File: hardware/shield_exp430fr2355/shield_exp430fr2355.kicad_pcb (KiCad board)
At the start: 2 copper layers, 34.3 x 50.8 mm, 51 parts, among them J1 TI_BOOSTER_40_J1, J10 Conn_01x02_Male, J11 Conn_01x04_Male, J12 Conn_01x02_Male, J13 Conn_01x02_Male, J14 Conn_01x02_Male, J15 Conn_01x02_Male, J16 Conn_01x02_Male, J17 Conn_01x02_Male, J18 Conn_01x02_Male, J19 Conn_01x02_Male, J2 TI_BOOSTER_40_J2, J20 Conn_01x02_Male, J21 Conn_01x02_Male, J22 Conn_01x02_Male, J23 Conn_01x02_Male, J24 Conn_01x02_Male, J25 Conn_01x02_Male, J27 Conn_01x02_Male, J28 Conn_01x02_Male, J3 TI_BOOSTER_40_J3, J4 TI_BOOSTER_40_J4, J6 Conn_02x13_Odd_Even, J7 Conn_01x02_Male, J8 Conn_01x02_Male, J9 Conn_01x02_Male, Q1 2N7002, Q2 2N7002, U1 NCP1117-3.3_SOT223

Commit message: Finished schematic
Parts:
- removed J11: Conn_01x04_Male, Connector_PinHeader_2.54mm:PinHeader_1x04_P2.54mm_Vertical
- D3, D4, U1: moved to B.Cu
- moved J12 157.1 mm to (309.6, 150.1)
- moved J21 145.8 mm to (308.9, 131.8)
- moved R14 144.5 mm to (267.8, 175.0)
- moved D1 143.6 mm to (314.6, 152.0)
- moved R15 143.3 mm to (267.7, 171.2)
- moved D2 139.2 mm to (314.5, 134.5)
- moved J28 128.1 mm to (256.0, 172.7)
- moved Q2 122.7 mm to (262.9, 174.1)
- moved J23 110.5 mm to (278.9, 128.7)
- moved J22 110.2 mm to (278.9, 120.0)
- moved R11 107.5 mm to (283.3, 127.9), turned to 180 degrees
- moved R7 105.4 mm to (283.3, 131.2)
- moved R10 100.3 mm to (282.4, 122.4), turned to 180 degrees
- moved R6 97.3 mm to (282.6, 119.8)
- moved R12 92.5 mm to (214.5, 160.3)
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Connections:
- net Net-(J1-Pad5) renamed P3.6
- net Net-(J1-Pad6) renamed P5.2
- net Net-(J1-Pad7) renamed P4.5
- net Net-(J1-Pad8) renamed P3.4
- net Net-(J2-Pad10) renamed P3.0
- net Net-(J2-Pad4) renamed P4.0
- net Net-(J2-Pad5) renamed RST
- net Net-(J2-Pad6) renamed P4.6
- net Net-(J2-Pad7) renamed P4.7
- net Net-(J2-Pad8) renamed P4.4
- net Net-(J3-Pad10) renamed P3.1
- net Net-(J3-Pad4) renamed P5.3
- net Net-(J3-Pad9) renamed P3.5
- net Net-(J4-Pad10) renamed P3.2
- net Net-(J4-Pad6) renamed P6.4
- net Net-(J4-Pad7) renamed P3.7
- net Net-(J4-Pad9) renamed P3.3
- D1 pad 3: P1.0 -> P1.1
- D2 pad 3: P1.3 -> P1.2
- J1 pad 1: VCC -> +3V3
- J1 pad 10: Net-(J1-Pad10) -> P1.2
- J1 pad 2: Net-(J1-Pad2) -> P1.5
- J1 pad 3: Net-(J1-Pad3) -> P1.6
- J1 pad 4: Net-(J1-Pad4) -> P1.7
- J1 pad 9: Net-(J1-Pad9) -> P1.3
- J12 pad 2: P1.0 -> P1.1
- J14 pad 2: P1.4 -> P2.2
- J15 pad 2: P2.1 -> P6.0
- J16 pad 2: P2.2 -> P6.1
- J17 pad 2: P2.4 -> P6.2
- J18 pad 2: P2.5 -> P6.3
- J2 pad 2: Net-(J2-Pad2) -> P2.0
- J2 pad 3: Net-(J2-Pad3) -> P2.2
- J2 pad 9: Net-(J2-Pad9) -> P2.5
- J20 pad 2: P1.7 -> P2.3
- J21 pad 2: P1.3 -> P1.2
- J24 pad 2: P2.0 -> P5.4
- J25 pad 2: P2.3 -> P2.4
- J3 pad 3: Net-(J3-Pad3) -> P1.4
- J3 pad 5: Net-(J3-Pad5) -> P5.1
- J3 pad 6: Net-(J3-Pad6) -> P5.0
- J3 pad 7: Net-(J3-Pad7) -> P5.4
- J3 pad 8: Net-(J3-Pad8) -> P1.1
- J4 pad 1: Net-(J4-Pad1) -> P2.1
- J4 pad 2: Net-(J4-Pad2) -> P6.0
- J4 pad 3: Net-(J4-Pad3) -> P6.1
- J4 pad 4: Net-(J4-Pad4) -> P6.2
- J4 pad 5: Net-(J4-Pad5) -> P6.3
- J4 pad 8: Net-(J4-Pad8) -> P2.4
- Q1 pad 2: P1.2 -> P1.7
- Q2 pad 2: P1.1 -> P1.6
- R1 pad 2: P1.5 -> P2.0
- R10 pad 1: P2.6 -> P5.0
- R11 pad 1: P2.7 -> P5.1
- R12 pad 2: P1.2 -> P1.7
- R14 pad 2: P1.1 -> P1.6
- R3 pad 1: P1.5 -> P2.0
- R4 pad 2: P1.6 -> P2.1
- R5 pad 1: P1.6 -> P2.1
- R6 pad 2: P2.6 -> P5.0
- R7 pad 2: P2.7 -> P5.1
- R8 pad 1: P2.0 -> P5.4
- R9 pad 1: P2.3 -> P2.4
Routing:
- net PWM1: track 0.00 -> 83.4 mm
- net PWM1N: track 0.00 -> 81.0 mm
- net PWM2: track 0.00 -> 76.4 mm
- net PWM2N: track 0.00 -> 75.6 mm
- net +5V: track 0.00 -> 47.9 mm
- net Net-(C1-Pad1): track 0.00 -> 24.2 mm
- net +3V3: track 0.00 -> 13.2 mm, vias 0 -> 2
- net P6.3: track 0.00 -> 5.35 mm
- net P6.2: track 0.00 -> 5.14 mm
- net P6.1: track 0.00 -> 4.92 mm
- net P6.0: track 0.00 -> 4.73 mm
- net GND: track 0.00 -> 3.59 mm
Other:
- board size 34.3 x 50.8 mm -> 74.6 x 50 mm
- net class Default: clearance 0.254 -> 0.3048; trace_width 0.254 -> 0.508; via_dia 0.889 -> 1.5; via_drill 0.635 -> 0.6
- rule trace_clearance: 0.254 -> 0.3048

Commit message: Routing tracks
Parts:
- C1, C2, D1, D2, Q1, Q2, R1, R10, R11, R12, R13, R14, R15, R3, R4, R5, R6, R7, R8, R9: moved to B.Cu
- moved D2 108.3 mm to (208.5, 156.9), turned to 270 degrees
- moved D1 106.0 mm to (208.5, 151.8), turned to 270 degrees
- moved R1 104.6 mm to (209.9, 160.9), turned to 90 degrees
- moved R3 103.7 mm to (207.5, 160.9), turned to 270 degrees
- moved J20 101.8 mm to (237.5, 162.5), turned to 180 degrees
- moved J13 98.2 mm to (215.6, 160.4), turned to 270 degrees
- moved J21 96.8 mm to (215.3, 156.7), turned to 270 degrees
- moved J12 94.3 mm to (215.4, 152.5), turned to 270 degrees
- moved J14 93.7 mm to (215.4, 144.8), turned to 270 degrees
- moved R15 84.7 mm to (185.2, 152.0), turned to 270 degrees
- moved R14 84.0 mm to (188.3, 148.0)
- moved J25 83.2 mm to (215.3, 141.1), turned to 270 degrees
- moved D5 81.2 mm to (217.7, 124.9)
- moved R6 79.5 mm to (208.5, 148.8), turned to 180 degrees
- moved R9 79.4 mm to (208.9, 141.1), turned to 180 degrees
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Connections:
- J20 pad 2: P2.3 -> P2.4
- J6 pad 18: GND -> Net-(J6-Pad18)
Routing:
- net R_TCRT: track 0.00 -> 110.1 mm, vias 0 -> 1
- net L_TCRT: track 0.00 -> 99.1 mm, vias 0 -> 1
- net D1: track 0.00 -> 95.4 mm, vias 0 -> 1
- net Trig0: track 0.00 -> 84.3 mm, vias 0 -> 1
- net D0: track 0.00 -> 70.8 mm, vias 0 -> 1
- net Echo1: track 0.00 -> 65.6 mm, vias 0 -> 1
- net Trig1: track 0.00 -> 61.8 mm, vias 0 -> 1
- net ADC0: track 0.00 -> 57.9 mm, vias 0 -> 2
- net +3V3: track 13.2 -> 68.6 mm, vias 2 -> 4
- net ADC1: track 0.00 -> 54.4 mm, vias 0 -> 2
- net Echo0: track 0.00 -> 51.0 mm, vias 0 -> 2
- net ADC2: track 0.00 -> 48.8 mm, vias 0 -> 2
- net ADC3: track 0.00 -> 32.9 mm, vias 0 -> 2
- net AMP2: track 0.00 -> 31.7 mm
- net P1.6: track 0.00 -> 19.9 mm
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- added copper zone on B.Cu, net GND
- added copper zone on F.Cu, net GND
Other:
- net class +5V added: clearance 0.3048, trace_width 0.7, via_dia 1.5, via_drill 0.6

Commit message: FR2355 interface board finished
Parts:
- removed J19, J20, J25: Conn_01x02_Male, Connector_PinHeader_2.54mm:PinHeader_1x02_P2.54mm_Vertical
- added ECHO1: Conn_01x02_Male, Connector_PinHeader_2.54mm:PinHeader_1x02_P2.54mm_Vertical, F.Cu at (237.0, 162.7)
- added L ESQ: Conn_01x02_Male, Connector_PinHeader_2.54mm:PinHeader_1x02_P2.54mm_Vertical, F.Cu at (215.3, 141.1)
- added TRIG1: Conn_01x02_Male, Connector_PinHeader_2.54mm:PinHeader_1x02_P2.54mm_Vertical, F.Cu at (240.6, 162.7)
- R ESQ: renamed from J24
- moved D5 33.3 mm to (185.6, 134.1)
- moved R2 33.3 mm to (185.6, 136.9)
- moved R4 23.8 mm to (233.2, 130.2), turned to 270 degrees
- moved R5 20.7 mm to (235.7, 130.2), turned to 90 degrees
- moved R10 1.41 mm to (207.7, 144.9), turned to 90 degrees
- moved TX 0.79 mm to (187.6, 160.2)
- moved R9 0.63 mm to (208.8, 141.7)
- moved R1 0.50 mm to (210.4, 160.9), turned to 270 degrees
- renumbered J12 to ADC0, J21 to ADC1, J13 to ECHO0, J22 to ENC0, J23 to ENC1, J15 to M1, J16 to M1N, J17 to M2, J18 to M2N, J28 to RX, J14 to TRIG0, J27 to TX
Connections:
- D5 pad 2: Net-(C1-Pad1) -> +3V3
- R9 pad 1: P2.4 -> P3.0
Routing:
- net GND: track 9.35 -> 106.3 mm, vias 4 -> 15
- net P2.0: track 2.39 -> 79.7 mm, vias 0 -> 2
- net P2.2: track 0.00 -> 64.3 mm, vias 0 -> 2
- net P3.0: track 0.00 -> 53.2 mm, vias 0 -> 2
- net D0: track 70.8 -> 122.1 mm, vias 1 -> 3
- net Trig1: track 61.8 -> 108.4 mm, vias 1 -> 2
- net Echo1: track 65.6 -> 110.0 mm, vias 1 -> 2
- net Net-(J19-Pad2): track 0.00 -> 41.3 mm, vias 0 -> 2
- net +3V3: track 68.6 -> 109.0 mm, vias 4 -> 6
- net P5.4: track 3.39 -> 22.7 mm, vias 0 -> 2
- net ADC1: track 54.4 -> 71.7 mm, vias 2 -> 3
- net ADC0: track 57.9 -> 73.4 mm
- net P5.1: track 2.16 -> 12.5 mm
- net P2.4: track 2.95 -> 13.2 mm
- net Echo0: track 51.0 -> 61.1 mm
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
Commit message: Added board documentation
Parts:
- removed J7: Conn_01x02_Male, Connector_PinHeader_2.54mm:PinHeader_1x02_P2.54mm_Vertical
- added POWER: Conn_01x02_Male, Connector_PinHeader_2.54mm:PinHeader_1x02_P2.54mm_Vertical, F.Cu at (188.5, 140.8)
- moved R2 3.93 mm to (185.6, 133.0), turned to 180 degrees
- moved D5 1.36 mm to (185.6, 135.5)
- moved ADC2 0.72 mm to (173.9, 126.2)
- renumbered J8 to ADC2, J9 to AMP1, J10 to AMP2
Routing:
- net Net-(C1-Pad1): track 23.3 -> 42.6 mm, vias 0 -> 2
- net GND: track 106.3 -> 93.8 mm, vias 15 -> 16
- net +3V3: track 109.0 -> 115.9 mm, vias 6 -> 7
- net ADC3: track 32.9 -> 31.3 mm
- net Echo1: track 110.0 -> 110.8 mm
- net ADC2: track 48.8 -> 49.5 mm
- net Trig1: track 108.4 -> 107.8 mm
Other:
- board text added: "ADC3"

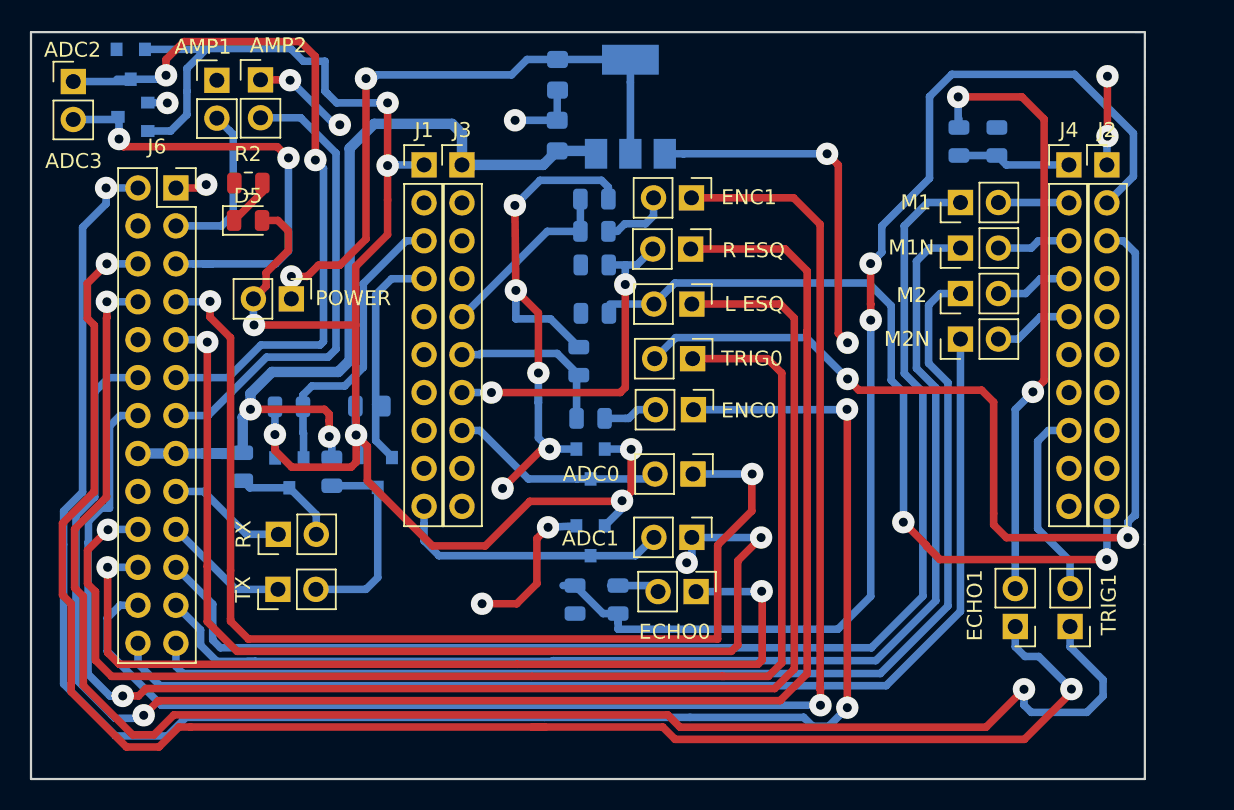
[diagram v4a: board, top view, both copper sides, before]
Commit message: Added 3d models, corrected PCB dimensions
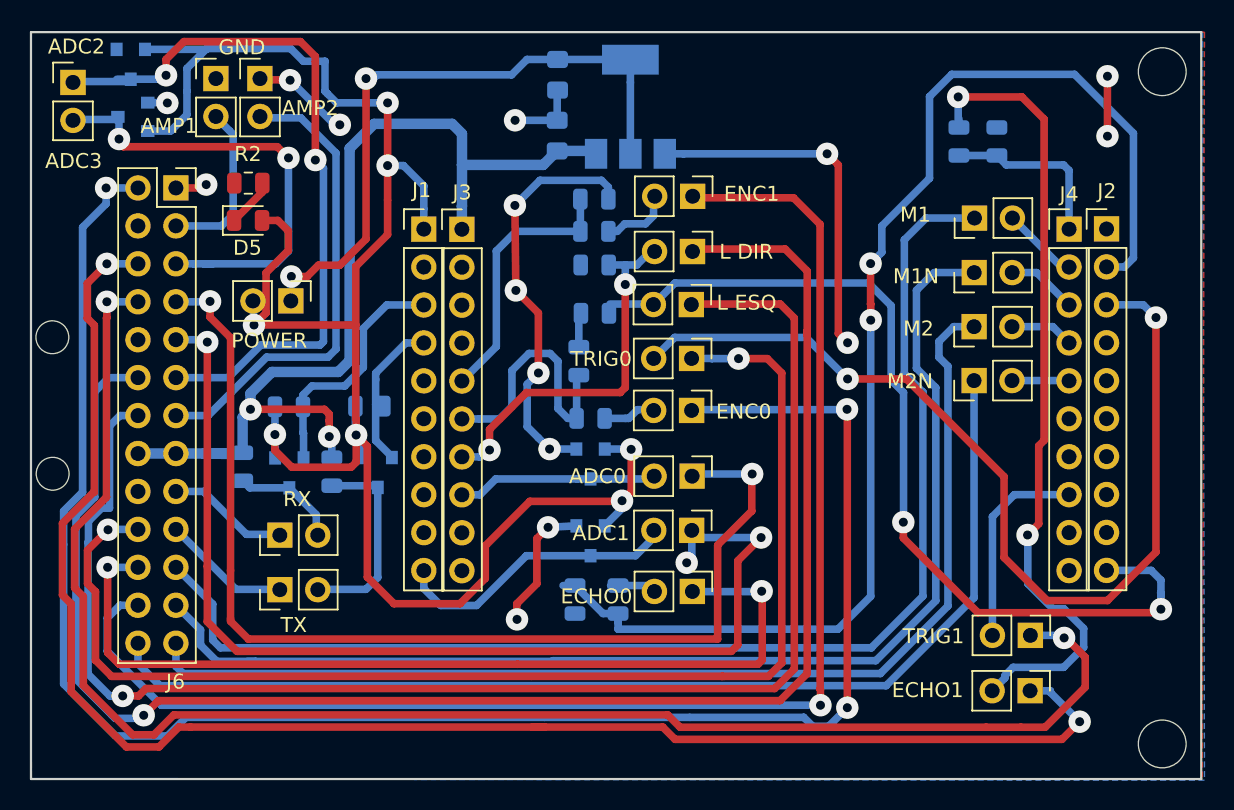
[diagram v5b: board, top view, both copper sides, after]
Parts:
- removed ADC0, ADC1, ADC2, AMP1, AMP2, ECHO0, ECHO1, ENC0, ENC1, M1, M1N, M2, M2N, POWER, RX, TRIG0, TRIG1, TX: Conn_01x02_Male, Connector_PinHeader_2.54mm:PinHeader_1x02_P2.54mm_Vertical
- removed L ESQ: Conn_01x02_Male, Connector_PinHeader_2.54mm:PinHeader_1x02_P2.54mm_Vertical
- removed R ESQ: Conn_01x02_Male, Connector_PinHeader_2.54mm:PinHeader_1x02_P2.54mm_Vertical
- added H1: MountingHole, MountingHole:MountingHole_2.2mm_M2, F.Cu at (172.5, 143.3)
- added H2: MountingHole, MountingHole:MountingHole_2.2mm_M2, F.Cu at (172.5, 152.5)
- added H3: MountingHole, MountingHole:MountingHole_3.2mm_M3, F.Cu at (246.8, 170.6)
- added H4: MountingHole, MountingHole:MountingHole_3.2mm_M3, F.Cu at (246.8, 125.5)
- added J10: Conn_01x02_Male, Connector_PinHeader_2.54mm:PinHeader_1x02_P2.54mm_Vertical, F.Cu at (186.4, 126.0)
- added J12: Conn_01x02_Male, Connector_PinHeader_2.54mm:PinHeader_1x02_P2.54mm_Vertical, F.Cu at (215.3, 152.6)
- added J13: Conn_01x02_Male, Connector_PinHeader_2.54mm:PinHeader_1x02_P2.54mm_Vertical, F.Cu at (215.3, 160.3)
- added J14: Conn_01x02_Male, Connector_PinHeader_2.54mm:PinHeader_1x02_P2.54mm_Vertical, F.Cu at (215.3, 144.7)
- added J15: Conn_01x02_Male, Connector_PinHeader_2.54mm:PinHeader_1x02_P2.54mm_Vertical, F.Cu at (234.2, 135.3)
- added J16: Conn_01x02_Male, Connector_PinHeader_2.54mm:PinHeader_1x02_P2.54mm_Vertical, F.Cu at (234.2, 139.0)
- added J17: Conn_01x02_Male, Connector_PinHeader_2.54mm:PinHeader_1x02_P2.54mm_Vertical, F.Cu at (234.2, 142.6)
- added J18: Conn_01x02_Male, Connector_PinHeader_2.54mm:PinHeader_1x02_P2.54mm_Vertical, F.Cu at (234.2, 146.2)
- added J19: Conn_01x02_Male, Connector_PinHeader_2.54mm:PinHeader_1x02_P2.54mm_Vertical, F.Cu at (238.0, 167.0)
- added J20: Conn_01x02_Male, Connector_PinHeader_2.54mm:PinHeader_1x02_P2.54mm_Vertical, F.Cu at (238.0, 163.3)
- added J21: Conn_01x02_Male, Connector_PinHeader_2.54mm:PinHeader_1x02_P2.54mm_Vertical, F.Cu at (215.3, 156.2)
- added J22: Conn_01x02_Male, Connector_PinHeader_2.54mm:PinHeader_1x02_P2.54mm_Vertical, F.Cu at (215.3, 148.2)
- added J23: Conn_01x02_Male, Connector_PinHeader_2.54mm:PinHeader_1x02_P2.54mm_Vertical, F.Cu at (215.4, 133.9)
- added J24: Conn_01x02_Male, Connector_PinHeader_2.54mm:PinHeader_1x02_P2.54mm_Vertical, F.Cu at (215.4, 137.6)
- added J25: Conn_01x02_Male, Connector_PinHeader_2.54mm:PinHeader_1x02_P2.54mm_Vertical, F.Cu at (215.3, 141.1)
- added J27: Conn_01x02_Male, Connector_PinHeader_2.54mm:PinHeader_1x02_P2.54mm_Vertical, F.Cu at (187.7, 160.2)
- added J28: Conn_01x02_Male, Connector_PinHeader_2.54mm:PinHeader_1x02_P2.54mm_Vertical, F.Cu at (187.7, 156.6)
- added J7: Conn_01x02_Male, Connector_PinHeader_2.54mm:PinHeader_1x02_P2.54mm_Vertical, F.Cu at (188.5, 140.9)
- added J8: Conn_01x02_Male, Connector_PinHeader_2.54mm:PinHeader_1x02_P2.54mm_Vertical, F.Cu at (173.9, 126.3)
- added J9: Conn_01x02_Male, Connector_PinHeader_2.54mm:PinHeader_1x02_P2.54mm_Vertical, F.Cu at (183.4, 126.0)
- moved J3 4.31 mm to (199.9, 136.1)
- moved J1 4.30 mm to (197.4, 136.1)
- moved J4 4.30 mm to (240.6, 136.1)
- moved J2 4.29 mm to (243.1, 136.1)
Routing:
- net +3V3: track 115.9 -> 129.4 mm
- net Net-(J19-Pad2): track 41.3 -> 54.3 mm
- net GND: track 93.8 -> 82.6 mm, vias 16 -> 15
- net P3.0: track 53.2 -> 62.4 mm
- net P5.0: track 11.4 -> 17.6 mm
- net P5.1: track 12.5 -> 18.0 mm
- net P2.0: track 79.7 -> 84.7 mm
- net P1.7: track 15.6 -> 10.7 mm
- net +5V: track 64.3 -> 68.6 mm
- net P2.1: track 7.63 -> 11.7 mm
- net P1.6: track 19.9 -> 16.3 mm
- net P5.4: track 22.7 -> 25.5 mm
- net Echo1: track 110.8 -> 108.1 mm
- net PWM2: track 78.4 -> 76.0 mm
- net PWM2N: track 77.3 -> 74.9 mm
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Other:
- board size 74.6 x 50 mm -> 78.4 x 50 mm
- board text added: "ADC0"
- board text added: "ADC1"
- board text added: "ADC2"
- board text added: "AMP1"
- board text added: "AMP2"
- board text added: "ECHO0"
- board text added: "ECHO1"
- board text added: "ENC0"
- board text added: "ENC1"
- board text added: "GND"
- board text added: "L DIR"
- board text added: "L ESQ"
- board text added: "M1"
- board text added: "M1N"
- board text added: "M2"
- board text added: "M2N"
- board text added: "POWER"
- board text added: "RX"
- board text added: "TRIG0"
- board text added: "TRIG1"
- board text added: "TX"
